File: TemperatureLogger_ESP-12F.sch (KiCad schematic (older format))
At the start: 19 parts, among them J1 Power for additional devices, J2 Additional I2C device, J3 Barrel_Jack, J4 FTDI_Cable, SW1 GND_to_reset, SW2 GND_to_program, U1 ESP-12F, U2 MCP1700-3302E_TO92, U6 GY-B11(BMP-280)

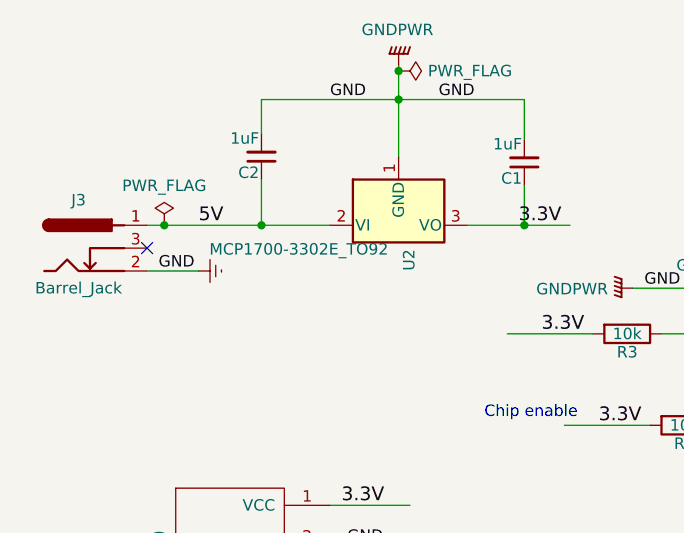
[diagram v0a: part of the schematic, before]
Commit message: Changing the linear regulator to the right one on the schematic to be able to use 9V batteries
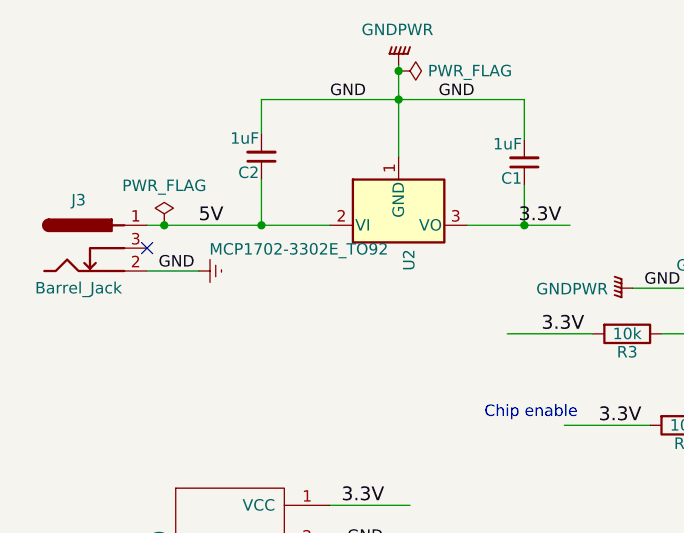
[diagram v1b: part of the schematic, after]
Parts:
- U2: value MCP1700-3302E_TO92 -> MCP1702-3302E_TO92
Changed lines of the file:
@@
 P 3150 1700
 F 0 "U2" V 3196 1595 50  0000 R CNN
-F 1 "MCP1700-3302E_TO92" H 3105 1595 50  0000 R CNN
+F 1 "MCP1702-3302E_TO92" H 3105 1595 50  0000 R CNN
 F 2 "Package_TO_SOT_THT:TO-92_Inline" H 3150 1500 50  0001 C CIN
-F 3 "http://ww1.microchip.com/downloads/en/DeviceDoc/20001826D.pdf" H 3150 1700 50  0001 C CNN
+F 3 "https://www.mouser.ca/datasheet/2/268/22008a-53656.pdf" H 3150 1700 50  0001 C CNN
 	1    3150 1700
 	1    0    0    -1

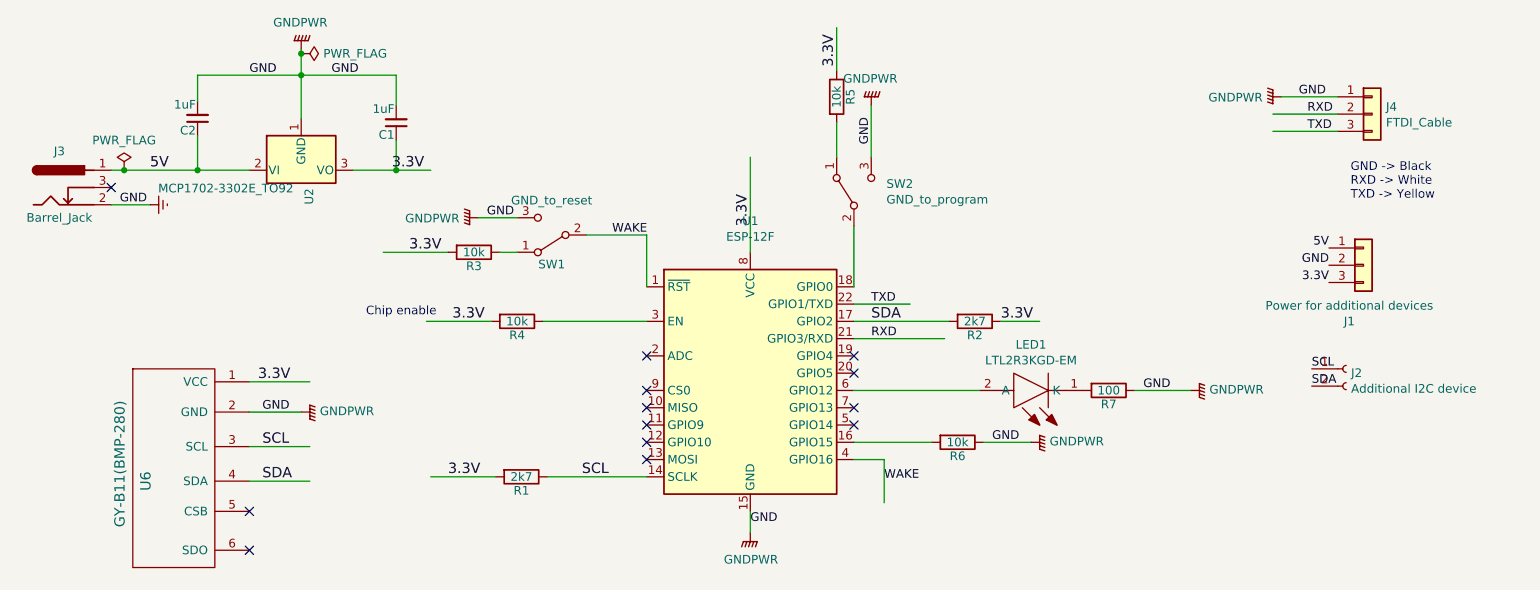
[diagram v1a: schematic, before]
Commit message: Correcting SDA to use GPIO14 instead of pin 14 of ESP8266
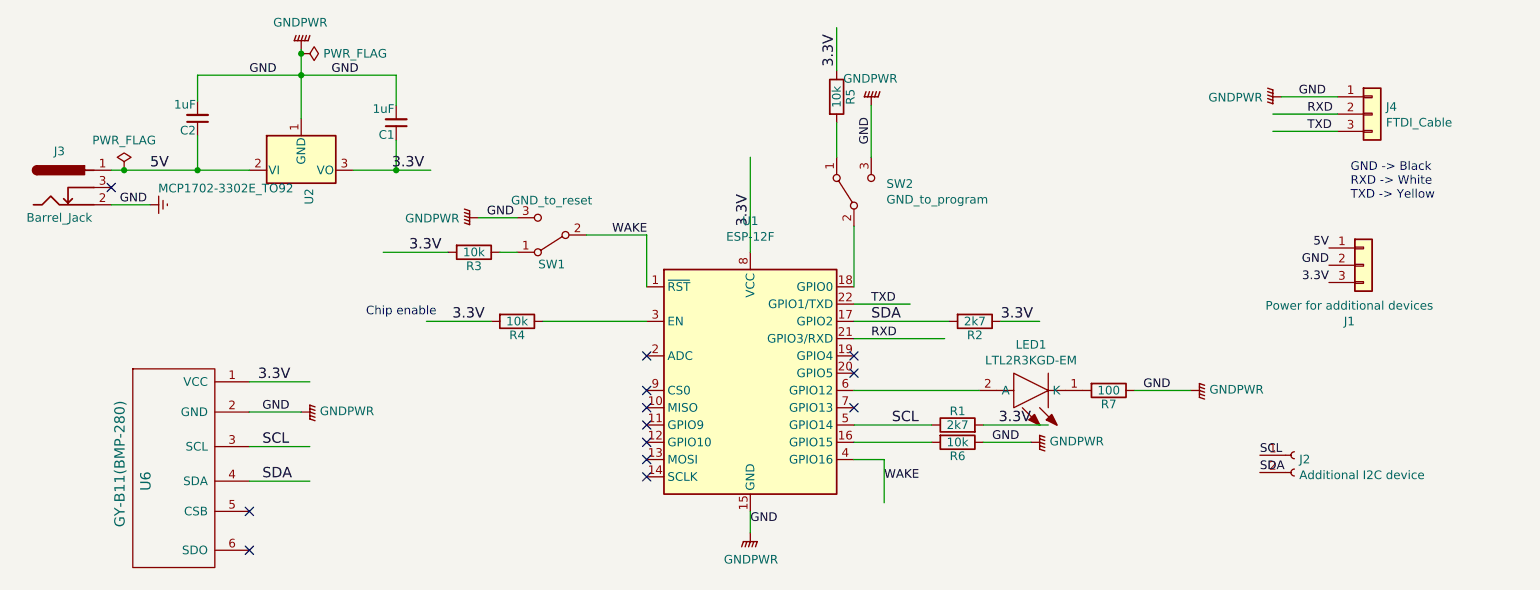
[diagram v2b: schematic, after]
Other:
- moved on the sheet: J2, R1
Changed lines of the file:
@@
 Comment4 ""
 $EndDescr
-Text Label 4775 3475 0    60   ~ 0
+Text Label 6725 3175 2    60   ~ 0
 SCL
 Text Label 6450 2575 0    60   ~ 0
@@
 $EndComp
 $Comp
-L TemperatureLogger_ESP-12F-rescue:R-ChickmaticPhase3-rescue R1
-U 1 1 59F5313A
-P 4425 3475
-F 0 "R1" V 4505 3475 50  0000 C CNN
-F 1 "2k7" V 4425 3475 50  0000 C CNN
-F 2 "Resistor_THT:R_Axial_DIN0204_L3.6mm_D1.6mm_P2.54mm_Vertical" V 4355 3475 50  0001 C CNN
-F 3 "" H 4425 3475 50  0001 C CNN
-	1    4425 3475
-	0    1    1    0
-$EndComp
-Text Label 4000 3475 0    60   ~ 0
-3.3V
-$Comp
 L TemperatureLogger_ESP-12F-rescue:R-ChickmaticPhase3-rescue R2
 U 1 1 59F53387
@@
 $EndComp
 Wire Wire Line
-	4575 3475 5150 3475
-Wire Wire Line
 	6350 2575 6900 2575
 Wire Wire Line
@@
 Wire Wire Line
 	5750 3675 5750 3800
-Wire Wire Line
-	4275 3475 3900 3475
 Wire Wire Line
 	7200 2575 7425 2575
@@
 Wire Wire Line
 	6350 3275 6800 3275
-Wire Wire Line
-	7100 3275 7375 3275
-Text Label 7150 3275 0    50   ~ 0
-GND
 $Comp
 L TemperatureLogger_ESP-12F-rescue:R-ChickmaticPhase3-rescue R5
@@
 Wire Wire Line
 	6250 1125 6250 875
-NoConn ~ 6350 3175
+NoConn ~ 5150 3475
 NoConn ~ 6350 3075
 NoConn ~ 6350 2875
@@
 $EndComp
 $Comp
-L power:GNDPWR #PWR0107
-U 1 1 5D078B85
-P 7375 3275
-F 0 "#PWR0107" H 7375 3075 50  0001 C CNN
-F 1 "GNDPWR" V 7380 3167 50  0000 R CNN
-F 2 "" H 7375 3225 50  0001 C CNN
-F 3 "" H 7375 3225 50  0001 C CNN
-	1    7375 3275
-	0    -1   -1   0
-$EndComp
-$Comp
 L power:GNDPWR #PWR0108
 U 1 1 5D07B0E8
@@
 $EndComp
 $Comp
+L power:PWR_FLAG #FLG0101
+U 1 1 5D082A4B
+P 3150 1025
+F 0 "#FLG0101" H 3150 1100 50  0001 C CNN
+F 1 "PWR_FLAG" V 3150 1153 50  0000 L CNN
+F 2 "" H 3150 1025 50  0001 C CNN
+F 3 "~" H 3150 1025 50  0001 C CNN
+	1    3150 1025
+	0    1    1    0
+$EndComp
+Connection ~ 3150 1025
+Wire Wire Line
+	3150 1025 3150 1000
+Text Notes 9225 1875 0    50   ~ 0
+GND -> Black\nRXD -> White\nTXD -> Yellow
+$Comp
+L Connector_Generic:Conn_01x03 J4
+U 1 1 5D090557
+P 9350 1375
+F 0 "J4" H 9430 1417 50  0000 L CNN
+F 1 "FTDI_Cable" H 9430 1326 50  0000 L CNN
+F 2 "Connector_PinHeader_2.54mm:PinHeader_1x03_P2.54mm_Vertical" H 9350 1375 50  0001 C CNN
+F 3 "~" H 9350 1375 50  0001 C CNN
+	1    9350 1375
+	1    0    0    -1
+$EndComp
+Text Label 9100 2350 2    50   ~ 0
+3.3V
+Text Label 9100 2150 2    50   ~ 0
+5V
+Text Label 9100 2250 2    50   ~ 0
+GND
+$Comp
+L Connector_Generic:Conn_01x03 J1
+U 1 1 5D08B684
+P 9300 2250
+F 0 "J1" H 9218 1925 50  0000 C CNN
+F 1 "Power for additional devices" H 9218 2016 50  0000 C CNN
+F 2 "Connector_PinHeader_2.54mm:PinHeader_1x03_P2.54mm_Vertical" H 9300 2250 50  0001 C CNN
+F 3 "~" H 9300 2250 50  0001 C CNN
+	1    9300 2250
+	1    0    0    -1
+$EndComp
+$Comp
+L power:GNDPWR #PWR0106
+U 1 1 5D077BEE
+P 8825 1275
+F 0 "#PWR0106" H 8825 1075 50  0001 C CNN
+F 1 "GNDPWR" V 8829 1166 50  0000 R CNN
+F 2 "" H 8825 1225 50  0001 C CNN
+F 3 "" H 8825 1225 50  0001 C CNN
+	1    8825 1275
+	0    1    1    0
+$EndComp
+Text Label 8975 1475 0    50   ~ 0
+TXD
+Text Label 8975 1375 0    50   ~ 0
+RXD
+Wire Wire Line
+	9150 1475 8775 1475
+Wire Wire Line
+	9150 1375 8775 1375
+Text Label 8925 1275 0    50   ~ 0
+GND
+Wire Wire Line
+	9150 1275 8825 1275
+Text Label 8700 3350 0    50   ~ 0
+SCL
+$Comp
+L Connector:Conn_01x02_Female J2
+U 1 1 5C99E4F7
+P 8900 3350
+F 0 "J2" H 8928 3326 50  0000 L CNN
+F 1 "Additional I2C device" H 8928 3235 50  0000 L CNN
+F 2 "Connector_PinHeader_2.54mm:PinHeader_1x02_P2.54mm_Vertical" H 8900 3350 50  0001 C CNN
+F 3 "~" H 8900 3350 50  0001 C CNN
+	1    8900 3350
+	1    0    0    -1
+$EndComp
+Text Label 8700 3450 0    50   ~ 0
+SDA
+$Comp
+L Switch:SW_SPDT SW2
+U 1 1 5DDA0686
+P 6350 1825
+F 0 "SW2" V 6396 1637 50  0000 R CNN
+F 1 "GND_to_program" V 6305 1637 50  0000 R CNN
+F 2 "TemperatureLogger_ESP-12F:EG1218" H 6350 1825 50  0001 C CNN
+F 3 "~" H 6350 1825 50  0001 C CNN
+	1    6350 1825
+	0    -1   -1   0
+$EndComp
+Wire Wire Line
+	6450 1325 6450 1625
+Wire Wire Line
+	6250 1425 6250 1625
+Wire Wire Line
+	6350 2025 6350 2375
+Wire Wire Line
+	2550 1150 3150 1150
+NoConn ~ 2850 3900
+Wire Wire Line
+	7100 3275 7375 3275
+$Comp
+L power:GNDPWR #PWR0107
+U 1 1 5D078B85
+P 7375 3275
+F 0 "#PWR0107" H 7375 3075 50  0001 C CNN
+F 1 "GNDPWR" V 7380 3167 50  0000 R CNN
+F 2 "" H 7375 3225 50  0001 C CNN
+F 3 "" H 7375 3225 50  0001 C CNN
+	1    7375 3275
+	0    -1   -1   0
+$EndComp
+Text Label 7150 3275 0    50   ~ 0
+GND
+Wire Wire Line
+	7100 3175 7475 3175
+Text Label 7375 3175 2    60   ~ 0
+3.3V
+$Comp
+L TemperatureLogger_ESP-12F-rescue:R-ChickmaticPhase3-rescue R1
+U 1 1 59F5313A
+P 6950 3175
+F 0 "R1" V 7030 3175 50  0000 C CNN
+F 1 "2k7" V 6950 3175 50  0000 C CNN
+F 2 "Resistor_THT:R_Axial_DIN0204_L3.6mm_D1.6mm_P2.54mm_Vertical" V 6880 3175 50  0001 C CNN
+F 3 "" H 6950 3175 50  0001 C CNN
+	1    6950 3175
+	0    -1   -1   0
+$EndComp
+$Comp
 L RF_Module:ESP-12F U1
 U 1 1 5CFE3763
@@
 	1    0    0    -1
 $EndComp
-$Comp
-L power:PWR_FLAG #FLG0101
-U 1 1 5D082A4B
-P 3150 1025
-F 0 "#FLG0101" H 3150 1100 50  0001 C CNN
-F 1 "PWR_FLAG" V 3150 1153 50  0000 L CNN
-F 2 "" H 3150 1025 50  0001 C CNN
-F 3 "~" H 3150 1025 50  0001 C CNN
-	1    3150 1025
-	0    1    1    0
-$EndComp
-Connection ~ 3150 1025
-Wire Wire Line
-	3150 1025 3150 1000
-Text Notes 9225 1875 0    50   ~ 0
-GND -> Black\nRXD -> White\nTXD -> Yellow
-$Comp
-L Connector_Generic:Conn_01x03 J4
-U 1 1 5D090557
-P 9350 1375
-F 0 "J4" H 9430 1417 50  0000 L CNN
-F 1 "FTDI_Cable" H 9430 1326 50  0000 L CNN
-F 2 "Connector_PinHeader_2.54mm:PinHeader_1x03_P2.54mm_Vertical" H 9350 1375 50  0001 C CNN
-F 3 "~" H 9350 1375 50  0001 C CNN
-	1    9350 1375
-	1    0    0    -1
-$EndComp
-Text Label 9100 2350 2    50   ~ 0
-3.3V
-Text Label 9100 2150 2    50   ~ 0
-5V
-Text Label 9100 2250 2    50   ~ 0
-GND
-$Comp
-L Connector_Generic:Conn_01x03 J1
-U 1 1 5D08B684
-P 9300 2250
-F 0 "J1" H 9218 1925 50  0000 C CNN
-F 1 "Power for additional devices" H 9218 2016 50  0000 C CNN
-F 2 "Connector_PinHeader_2.54mm:PinHeader_1x03_P2.54mm_Vertical" H 9300 2250 50  0001 C CNN
-F 3 "~" H 9300 2250 50  0001 C CNN
-	1    9300 2250
-	1    0    0    -1
-$EndComp
-$Comp
-L power:GNDPWR #PWR0106
-U 1 1 5D077BEE
-P 8825 1275
-F 0 "#PWR0106" H 8825 1075 50  0001 C CNN
-F 1 "GNDPWR" V 8829 1166 50  0000 R CNN
-F 2 "" H 8825 1225 50  0001 C CNN
-F 3 "" H 8825 1225 50  0001 C CNN
-	1    8825 1275
-	0    1    1    0
-$EndComp
-Text Label 8975 1475 0    50   ~ 0
-TXD
-Text Label 8975 1375 0    50   ~ 0
-RXD
-Wire Wire Line
-	9150 1475 8775 1475
-Wire Wire Line
-	9150 1375 8775 1375
-Text Label 8925 1275 0    50   ~ 0
-GND
-Wire Wire Line
-	9150 1275 8825 1275
-Text Label 9000 2850 0    50   ~ 0
-SCL
-$Comp
-L Connector:Conn_01x02_Female J2
-U 1 1 5C99E4F7
-P 9200 2850
-F 0 "J2" H 9228 2826 50  0000 L CNN
-F 1 "Additional I2C device" H 9228 2735 50  0000 L CNN
-F 2 "Connector_PinHeader_2.54mm:PinHeader_1x02_P2.54mm_Vertical" H 9200 2850 50  0001 C CNN
-F 3 "~" H 9200 2850 50  0001 C CNN
-	1    9200 2850
-	1    0    0    -1
-$EndComp
-Text Label 9000 2950 0    50   ~ 0
-SDA
-$Comp
-L Switch:SW_SPDT SW2
-U 1 1 5DDA0686
-P 6350 1825
-F 0 "SW2" V 6396 1637 50  0000 R CNN
-F 1 "GND_to_program" V 6305 1637 50  0000 R CNN
-F 2 "TemperatureLogger_ESP-12F:EG1218" H 6350 1825 50  0001 C CNN
-F 3 "~" H 6350 1825 50  0001 C CNN
-	1    6350 1825
-	0    -1   -1   0
-$EndComp
-Wire Wire Line
-	6450 1325 6450 1625
-Wire Wire Line
-	6250 1425 6250 1625
-Wire Wire Line
-	6350 2025 6350 2375
-Wire Wire Line
-	2550 1150 3150 1150
-NoConn ~ 2850 3900
+Wire Wire Line
+	6800 3175 6350 3175
 $EndSCHEMATC
